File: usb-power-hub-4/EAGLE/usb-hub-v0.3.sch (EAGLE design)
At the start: 37 parts, among them U1 RICHTEKRT9715AGBR, U2 RICHTEKRT9715AGBR, U3 RICHTEKRT9715AGBR, U4 RICHTEKRT9715AGBR

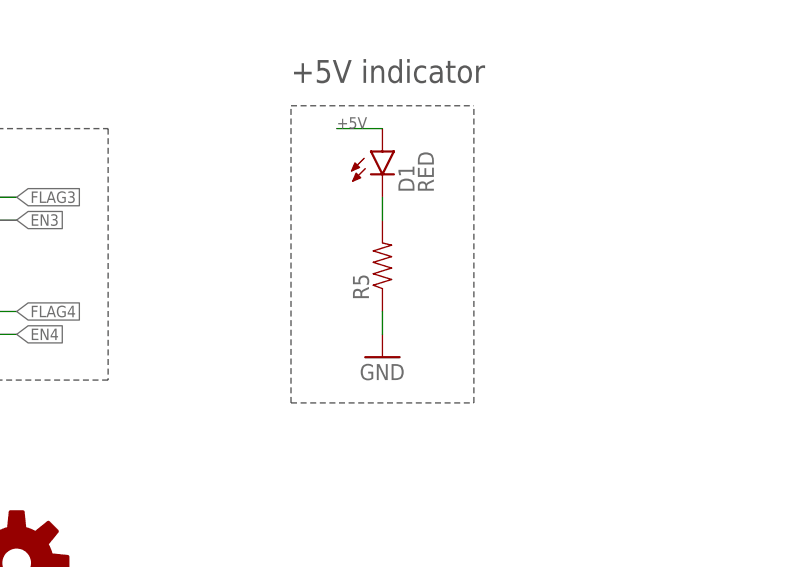
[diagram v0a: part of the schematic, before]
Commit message: added missing R5 value
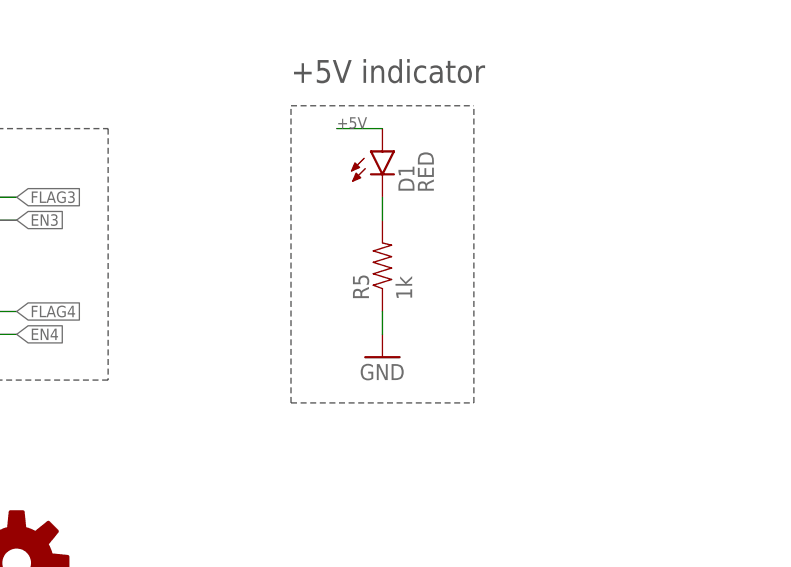
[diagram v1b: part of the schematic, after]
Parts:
- R5: value (none) -> 1k
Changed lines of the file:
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@@
 <attributes>
 <attribute name="CNAME" value="USB Power hub x4"/>
-<attribute name="CREVISION" value="V0.2"/>
+<attribute name="CREVISION" value="V0.2.1"/>
 <attribute name="DESIGNER" value="kennethlimcp"/>
 </attributes>
@@
 <part name="JP12" library="SparkFun-Connectors" deviceset="M02" device="PTH"/>
 <part name="D1" library="SparkFun-LED" deviceset="LED-RED" device="0603" value="RED"/>
-<part name="R5" library="SparkFun-Resistors" deviceset="RESISTOR" device="0402"/>
+<part name="R5" library="SparkFun-Resistors" deviceset="RESISTOR" device="0402" value="1k"/>
 <part name="GND3" library="SparkFun-Aesthetics" deviceset="GND" device=""/>
 </parts>
